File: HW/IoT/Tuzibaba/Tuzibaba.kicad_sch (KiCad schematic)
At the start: 3 parts

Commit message: Add changes made to schem and pcb
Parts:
- removed J?: 2x9 2.54mm 90deg female, symbol Connector_Generic:Conn_02x09_Counter_Clockwise
- added J1: 2x9 2.54mm 90deg female, Connector_PinSocket_2.54mm:PinSocket_2x09_P2.54mm_Vertical, symbol Connector_Generic:Conn_02x09_Odd_Even
- added R1, R2: 10K, For_Rasterboard:R_Axial_DIN0207_L6.3mm_D2.5mm_P7.62mm_Horizontal, symbol Device:R
- added R3, R4: 4.7K, For_Rasterboard:R_Axial_DIN0207_L6.3mm_D2.5mm_P7.62mm_Horizontal, symbol Device:R
- gave numbers to parts that had none: 1
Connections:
- net GND: now also A1.29 (GND), J1.1 (Pin_1)
- net D1: now reaches A1.10 (A1)
- net D1: now also J1.16 (Pin_16)
- net at A1.13 (SDA/A4): now also R1.2
- net at A1.14 (SCL/A5): now also R2.2
- net D7: now reaches A1.22 (D7)
- net D7: now also J1.10 (Pin_10)
- net at A1.26 (D11): now also R3.2
- net SIOD: now reaches A1.31 (SDA/A4)
- net SIOD: now also J1.3 (Pin_3)
- net SIOC: now reaches A1.32 (SCL/A5)
- net SIOC: now also J1.4 (Pin_4)
- net +3V3: now reaches A1.4 (3V3)
- net +3V3: now also J1.2 (Pin_2)
- net OUT0 renamed D0
- net D0: now also J1.15 (Pin_15)
- net PWM: no longer names the net of J2.3 (Pin_3)
- new net: R3.1, R4.1
- new net: R1.1, R2.1
- no-connect marks 7 -> 3
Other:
- moved on the sheet: A1, J2

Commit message: Finalizing schematic
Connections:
- net DIS0 is gone; now on net PCLK: A1.17 (D2)
- net +3V3: now also J1.18 (Pin_18), R1.2, R2.1
- net GND: now also J1.17 (Pin_17), R4.2
- net SIOC: now also R2.2
- net SIOD: now also R1.1
- net XCLK: now reaches R3.1, R4.1
- net XCLK: now also J1.7 (Pin_7)
- net S_XCLK: now reaches A1.26 (D11), R3.2
- net D2: now reaches A1.11 (A2)
- net D2: now also J1.13 (Pin_13)
- net D3: now reaches A1.12 (A3)
- net D3: now also J1.14 (Pin_14)
- net at A1.13 (SDA/A4): no longer R1.2
- net at A1.14 (SCL/A5): no longer R2.2
- net VSYN0: now reaches A1.18 (D3)
- net VSYN0: now also J1.6 (Pin_6)
- net D4: now reaches A1.19 (D4)
- net D4: now also J1.11 (Pin_11)
- net HREF: now reaches A1.23 (D8)
- net HREF: now also J1.5 (Pin_5)
- net D5: now reaches J1.12 (Pin_12)
- net PCLK: now reaches J1.8 (Pin_8)
- net D6: now reaches J1.9 (Pin_9)
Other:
- moved on the sheet: J1, J2, R1, R2, R3, R4

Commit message: Update schematic and pcb
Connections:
- net D5: now also A1.20 (D5)
- net D6: no longer J1.9 (Pin_9)
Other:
- moved on the sheet: J1, R3, R4

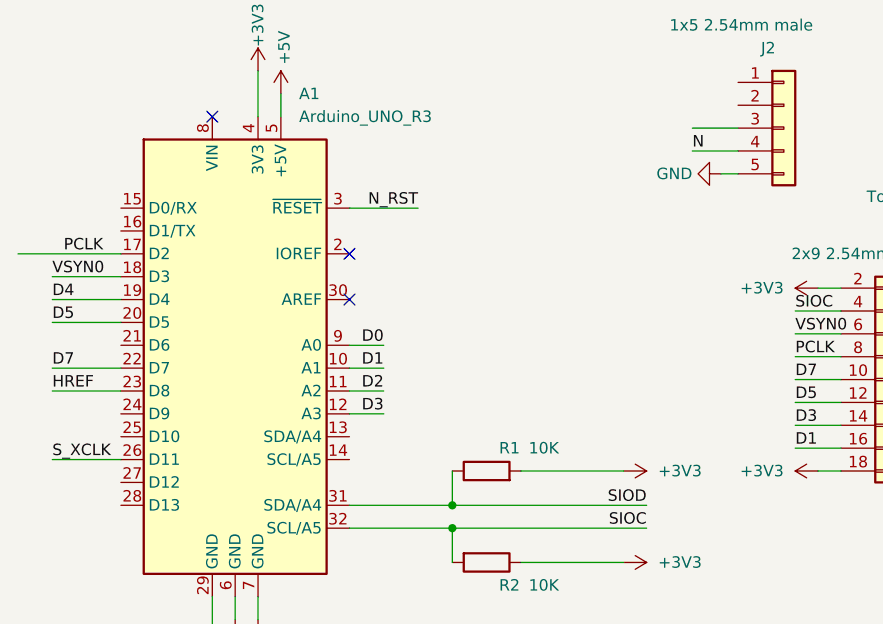
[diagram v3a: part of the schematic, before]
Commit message: Update schematic and pcb for camera
FOR IT IS FINALLY WORKING
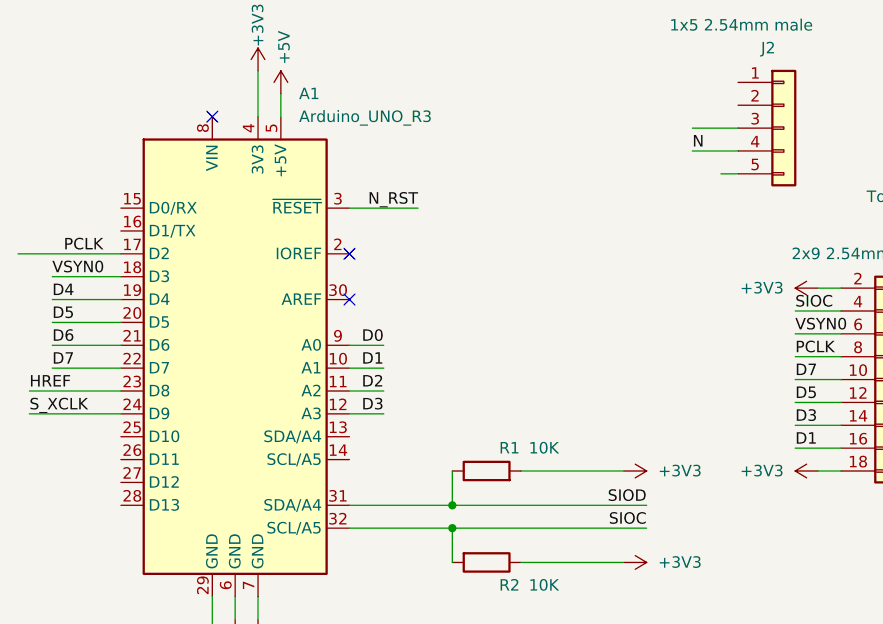
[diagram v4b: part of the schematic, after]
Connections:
- net D6: now also A1.21 (D6)
- net GND: no longer J2.5 (Pin_5)
- net S_XCLK: now also A1.24 (D9); no longer A1.26 (D11)
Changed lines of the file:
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@@
+    (stroke (width 0) (type default) (color 0 0 0 0))
+  )
+  (wire (pts (xy 77.47 86.36) (xy 87.63 86.36))
     (stroke (width 0) (type default) (color 0 0 0 0))
   )
@@
     (stroke (width 0) (type default) (color 0 0 0 0))
   )
-  (wire (pts (xy 80.01 83.82) (xy 87.63 83.82))
-    (stroke (width 0) (type default) (color 0 0 0 0))
-  )
   (wire (pts (xy 132.08 92.71) (xy 143.51 92.71))
     (stroke (width 0) (type default) (color 0 0 0 0))
@@
     (stroke (width 0) (type default) (color 0 0 0 0))
   )
-  (wire (pts (xy 80.01 91.44) (xy 87.63 91.44))
-    (stroke (width 0) (type default) (color 0 0 0 0))
-  )
   (wire (pts (xy 180.34 85.09) (xy 186.69 85.09))
     (stroke (width 0) (type default) (color 0 0 0 0))
@@
     (stroke (width 0) (type default) (color 0 0 0 0))
   )
+  (wire (pts (xy 77.47 83.82) (xy 87.63 83.82))
+    (stroke (width 0) (type default) (color 0 0 0 0))
+  )
   (wire (pts (xy 156.21 54.61) (xy 151.13 54.61))
     (stroke (width 0) (type default) (color 0 0 0 0))
   )
+  (wire (pts (xy 80.01 78.74) (xy 87.63 78.74))
+    (stroke (width 0) (type default) (color 0 0 0 0))
+  )
   (wire (pts (xy 113.03 86.36) (xy 116.84 86.36))
     (stroke (width 0) (type default) (color 0 0 0 0))
@@
     (effects (font (size 1.27 1.27)) (justify right bottom))
   )
-  (label "HREF" (at 80.01 83.82 0)
+  (label "HREF" (at 77.47 83.82 0)
     (effects (font (size 1.27 1.27)) (justify left bottom))
   )
@@
     (effects (font (size 1.27 1.27)) (justify right bottom))
   )
+  (label "D6" (at 80.01 78.74 0)
+    (effects (font (size 1.27 1.27)) (justify left bottom))
+  )
   (label "HREF" (at 185.42 77.47 180)
     (effects (font (size 1.27 1.27)) (justify right bottom))
@@
     (effects (font (size 1.27 1.27)) (justify right bottom))
   )
-  (label "S_XCLK" (at 80.01 91.44 0)
+  (label "S_XCLK" (at 77.47 86.36 0)
     (effects (font (size 1.27 1.27)) (justify left bottom))
   )
@@
     (pin "1")
     (pin "2")
-  )
-  (symbol (lib_id "power:GND") (at 154.305 59.69 270) (unit 1)
-    (in_bom yes) (on_board yes) (fields_autoplaced)
-    (property "Reference" "#PWR05" (id 0) (at 147.955 59.69 0)
-      (effects (font (size 1.27 1.27)) hide)
-    )
-    (property "Value" "GND" (id 1) (at 151.13 59.6899 90)
-      (effects (font (size 1.27 1.27)) (justify right))
-    )
-    (property "Footprint" "" (id 2) (at 154.305 59.69 0)
-      (effects (font (size 1.27 1.27)) hide)
-    )
-    (property "Datasheet" "" (id 3) (at 154.305 59.69 0)
-      (effects (font (size 1.27 1.27)) hide)
-    )
-    (pin "1")
   )
   (symbol (lib_id "power:GND") (at 184.15 72.39 90) (unit 1)
@@
       (reference "#PWR04") (unit 1) (value "+3V3") (footprint "")
     )
-    (path "/12ab01ac-451e-47bb-93c6-2c0bbfb0edfe"
-      (reference "#PWR05") (unit 1) (value "GND") (footprint "")
-    )
     (path "/1a5daa30-28ed-4713-803f-ae597390579c"

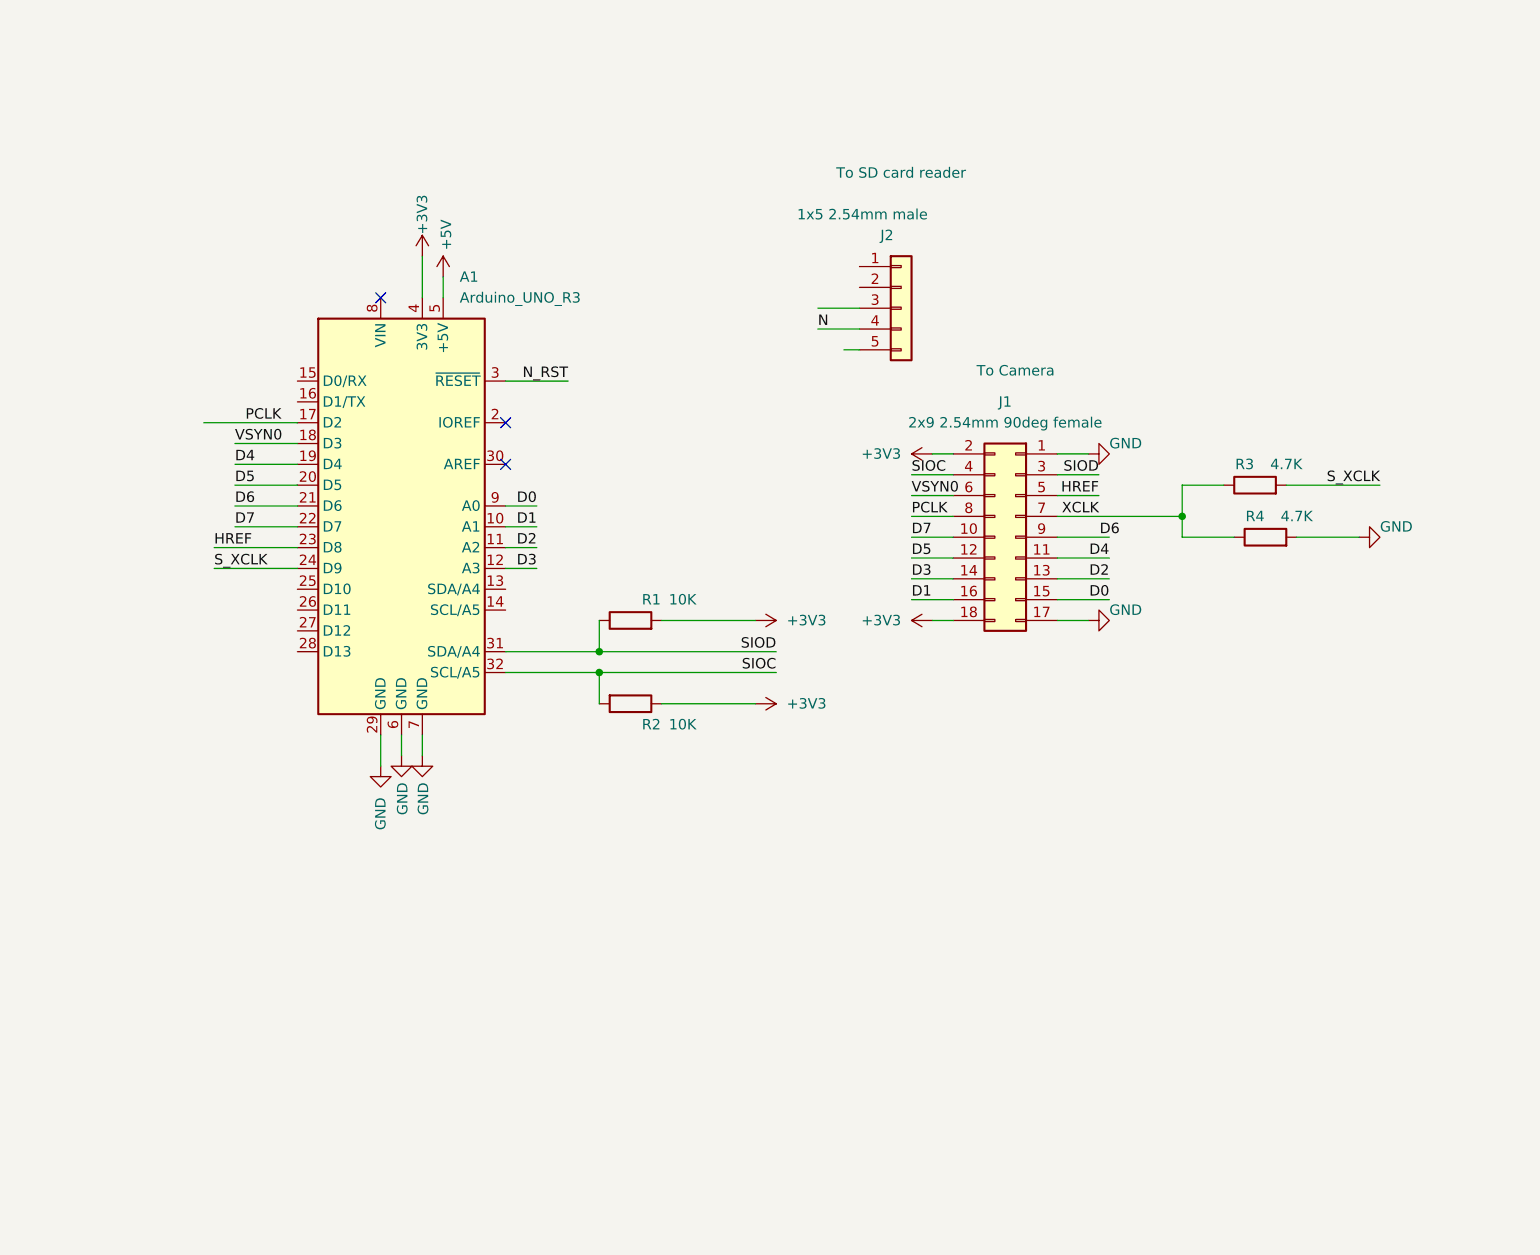
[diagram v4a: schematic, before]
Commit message: Finalize schematic and pcb for arduino with camera
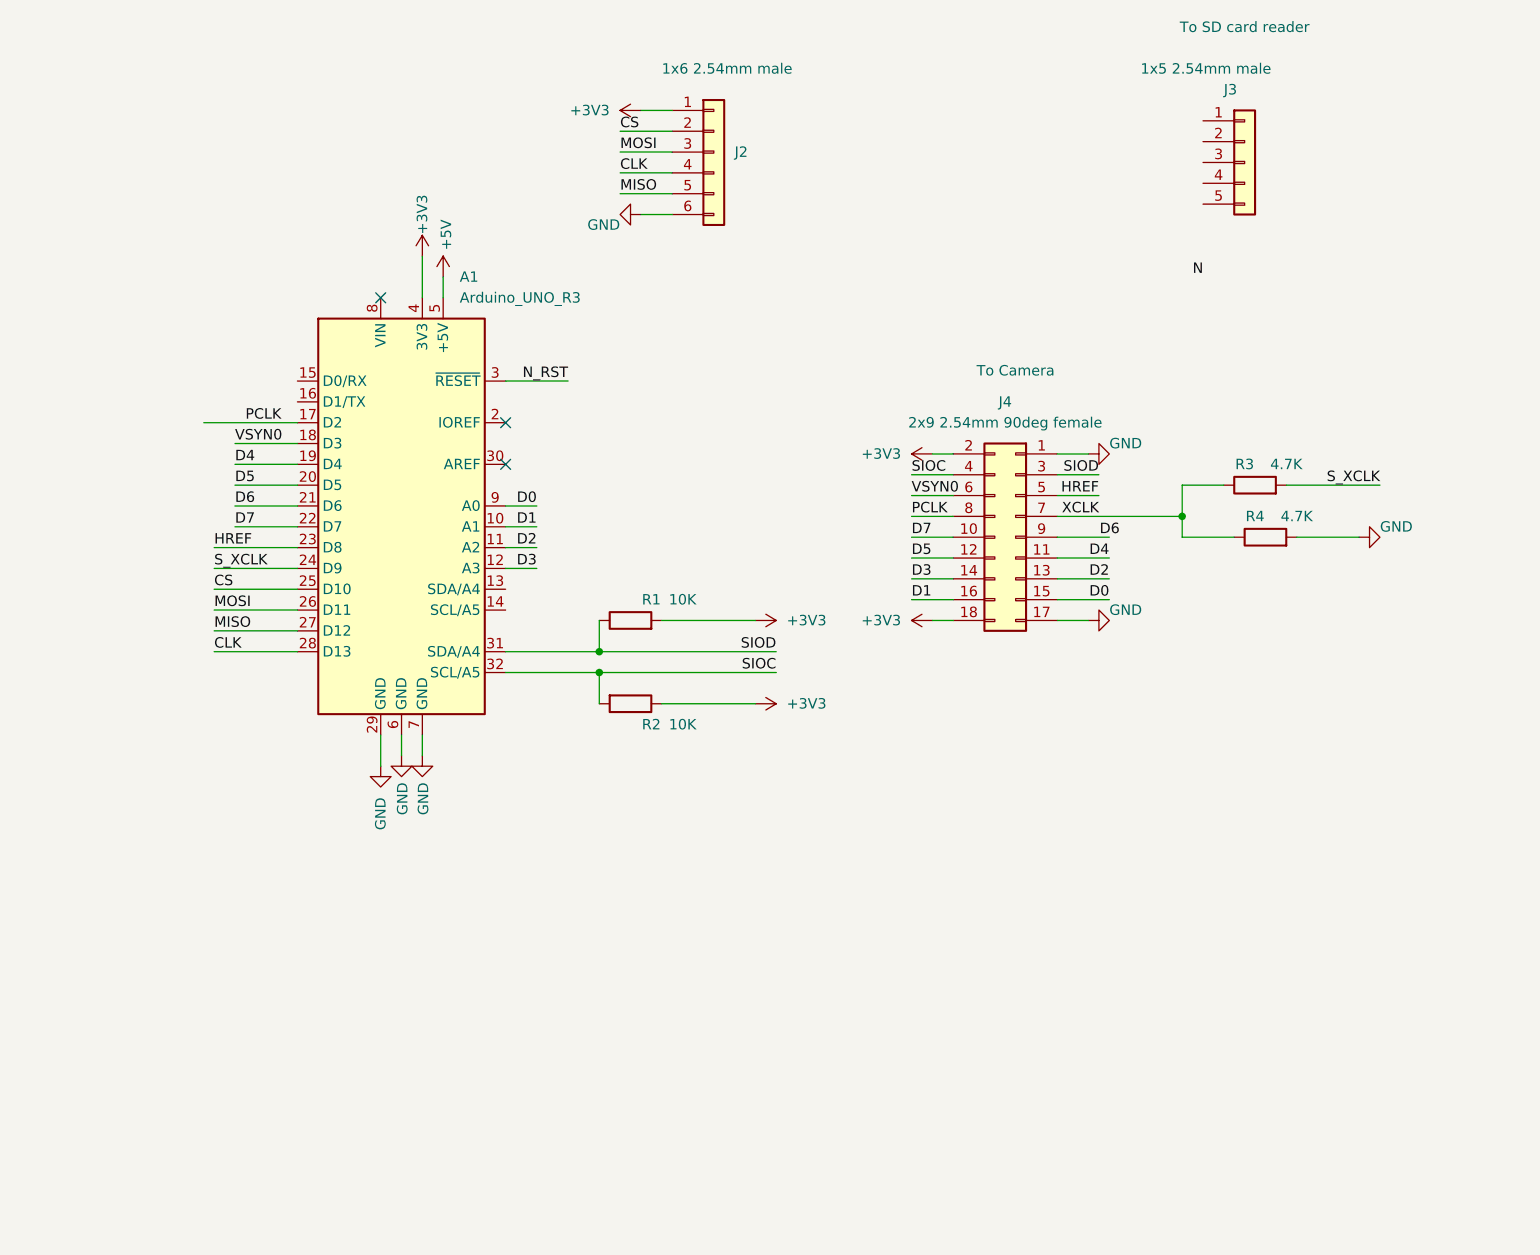
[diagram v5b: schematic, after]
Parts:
- added J2: 1x6 2.54mm male, Connector_PinSocket_2.54mm:PinSocket_1x06_P2.54mm_Vertical, symbol Tuzibaba-cache:Connector_Generic_Conn_01x06
- renumbered J2 to J3, J1 to J4
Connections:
- net +3V3: now also J2.1 (Pin_1)
- net GND: now also J2.6 (Pin_6)
- net N: no longer J3.4 (Pin_4)
- net CS: now reaches A1.25 (D10)
- net CS: now also J2.2 (Pin_2)
- net MOSI: now reaches A1.26 (D11)
- net MOSI: now also J2.3 (Pin_3)
- net MISO: now reaches A1.27 (D12)
- net MISO: now also J2.5 (Pin_5)
- net CLK: now reaches A1.28 (D13)
- net CLK: now also J2.4 (Pin_4)
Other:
- moved on the sheet: J3

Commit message: Add 3pin connector for UART w/ 2nd arduino
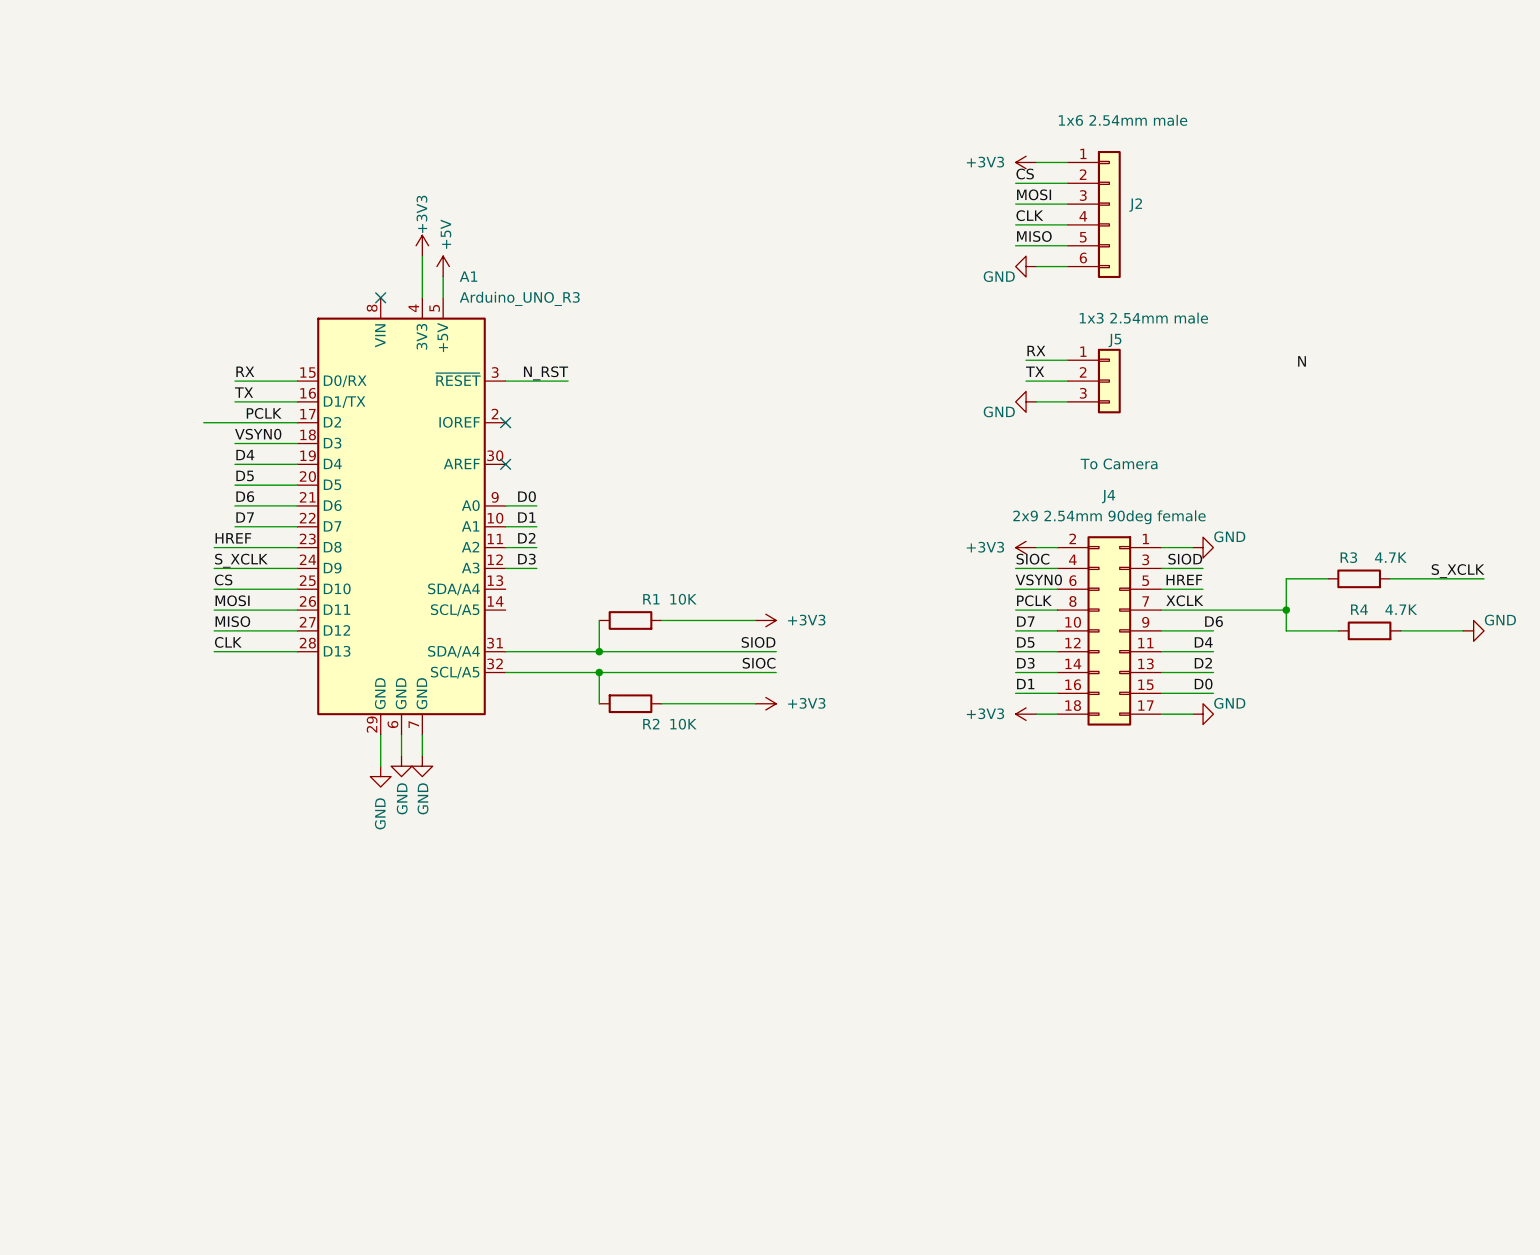
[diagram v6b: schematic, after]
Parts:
- removed J3: 1x5 2.54mm male, Connector_PinSocket_2.54mm:PinSocket_1x05_P2.54mm_Vertical, symbol Connector_Generic:Conn_01x05
- added J5: 1x3 2.54mm male, Connector_PinSocket_2.54mm:PinSocket_1x03_P2.54mm_Vertical, symbol Connector_Generic:Conn_01x03
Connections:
- net GND: now also J5.3 (Pin_3)
- net RX: now reaches A1.15 (D0/RX)
- net RX: now also J5.1 (Pin_1)
- net TX: now reaches A1.16 (D1/TX)
- net TX: now also J5.2 (Pin_2)
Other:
- moved on the sheet: J2, J4, R3, R4
